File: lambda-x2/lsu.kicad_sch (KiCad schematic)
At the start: 56 parts, among them Q5 BSS169H6327, Q6 BSS169H6327, Q7 BSS169H6327, Q8 BSS169H6327, U12 MCP6002T-I/SN, U3 MCP6002T-I/SN, U9 GS8332-SR

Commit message: cosmetic
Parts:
- TP10: value (none) -> Ip; footprint (none) -> TestPoint:TestPoint_Pad_D1.0mm
- TP11: value (none) -> Rtrim; footprint (none) -> TestPoint:TestPoint_Pad_D1.0mm
- TP12: value (none) -> Vm; footprint (none) -> TestPoint:TestPoint_Pad_D1.0mm
- TP3: value (none) -> Un_Sense; footprint (none) -> TestPoint:TestPoint_Pad_D1.0mm
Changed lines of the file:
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@@
       (effects (font (size 1.27 1.27)) (justify left) hide)
     )
-    (property "Value" "" (id 1) (at 172.72 113.03 0)
-      (effects (font (size 1.27 1.27)) (justify left))
-    )
-    (property "Footprint" "" (id 2) (at 175.26 116.84 0)
+    (property "Value" "Un_Sense" (id 1) (at 172.72 113.03 0)
+      (effects (font (size 1.27 1.27)) (justify left))
+    )
+    (property "Footprint" "TestPoint:TestPoint_Pad_D1.0mm" (id 2) (at 175.26 116.84 0)
       (effects (font (size 1.27 1.27)) hide)
     )
@@
       (effects (font (size 1.27 1.27)) (justify left) hide)
     )
-    (property "Value" "" (id 1) (at 83.82 213.36 0)
-      (effects (font (size 1.27 1.27)) (justify left))
-    )
-    (property "Footprint" "" (id 2) (at 86.36 217.17 0)
+    (property "Value" "Ip" (id 1) (at 83.82 213.36 0)
+      (effects (font (size 1.27 1.27)) (justify left))
+    )
+    (property "Footprint" "TestPoint:TestPoint_Pad_D1.0mm" (id 2) (at 86.36 217.17 0)
       (effects (font (size 1.27 1.27)) hide)
     )
@@
       (effects (font (size 1.27 1.27)) (justify left) hide)
     )
-    (property "Value" "" (id 1) (at 83.82 223.52 0)
-      (effects (font (size 1.27 1.27)) (justify left))
-    )
-    (property "Footprint" "" (id 2) (at 86.36 227.33 0)
+    (property "Value" "Rtrim" (id 1) (at 83.82 223.52 0)
+      (effects (font (size 1.27 1.27)) (justify left))
+    )
+    (property "Footprint" "TestPoint:TestPoint_Pad_D1.0mm" (id 2) (at 86.36 227.33 0)
       (effects (font (size 1.27 1.27)) hide)
     )
@@
       (effects (font (size 1.27 1.27)) (justify left) hide)
     )
-    (property "Value" "" (id 1) (at 85.09 67.31 0)
-      (effects (font (size 1.27 1.27)) (justify left))
-    )
-    (property "Footprint" "" (id 2) (at 87.63 71.12 0)
-      (effects (font (size 1.27 1.27)) hide)
-    )
+    (property "Value" "Vm" (id 1) (at 85.09 67.31 0)
+      (effects (font (size 1.27 1.27)) (justify left))
+    )
+    (property "Footprint" "TestPoint:TestPoint_Pad_D1.0mm" (id 2) (at 87.63 71.12 0)
+      (effects (font (size 1.27 1.27)) hide)
+    )

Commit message: Progress
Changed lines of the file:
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@@
     (pin "2")
   )
-  (symbol (lib_id "power:GND") (at 222.25 264.16 0) (unit 1)
+  (symbol (lib_name "GND_6") (lib_id "power:GND") (at 222.25 264.16 0) (unit 1)
     (in_bom yes) (on_board yes)
     (property "Reference" "#PWR0104" (id 0) (at 222.25 270.51 0)
       (effects (font (size 1.27 1.27)) hide)
     )
-    (property "Value" "GND" (id 1) (at 222.377 268.5542 0))
+    (property "Value" "" (id 1) (at 222.377 268.5542 0)
+      (effects (font (size 1.27 1.27)) hide)
+    )
     (property "Footprint" "" (id 2) (at 222.25 264.16 0)
       (effects (font (size 1.27 1.27)) hide)
@@
       (effects (font (size 1.27 1.27)) hide)
     )
-    (property "Value" "GND" (id 1) (at 117.983 131.3942 0))
+    (property "Value" "" (id 1) (at 117.983 131.3942 0)
+      (effects (font (size 1.27 1.27)) hide)
+    )
     (property "Footprint" "" (id 2) (at 118.11 127 0)
       (effects (font (size 1.27 1.27)) hide)
@@
     (pin "2")
   )
-  (symbol (lib_id "power:GND") (at 162.56 264.16 0) (mirror y) (unit 1)
+  (symbol (lib_name "GND_5") (lib_id "power:GND") (at 162.56 264.16 0) (mirror y) (unit 1)
     (in_bom yes) (on_board yes)
     (property "Reference" "#PWR0125" (id 0) (at 162.56 270.51 0)
       (effects (font (size 1.27 1.27)) hide)
     )
-    (property "Value" "GND" (id 1) (at 162.433 268.5542 0))
+    (property "Value" "" (id 1) (at 162.433 268.5542 0)
+      (effects (font (size 1.27 1.27)) hide)
+    )
     (property "Footprint" "" (id 2) (at 162.56 264.16 0)
       (effects (font (size 1.27 1.27)) hide)
@@
       (effects (font (size 1.27 1.27)) hide)
     )
-    (property "Value" "GND" (id 1) (at 222.25 172.72 0))
+    (property "Value" "" (id 1) (at 222.25 172.72 0)
+      (effects (font (size 1.27 1.27)) hide)
+    )
     (property "Footprint" "" (id 2) (at 222.25 168.91 0)
       (effects (font (size 1.27 1.27)) hide)
@@
     (pin "2")
   )
-  (symbol (lib_id "power:GND") (at 87.63 81.28 0) (mirror y) (unit 1)
+  (symbol (lib_name "GND_2") (lib_id "power:GND") (at 87.63 81.28 0) (mirror y) (unit 1)
     (in_bom yes) (on_board yes)
     (property "Reference" "#PWR0126" (id 0) (at 87.63 87.63 0)
       (effects (font (size 1.27 1.27)) hide)
     )
-    (property "Value" "GND" (id 1) (at 87.503 85.6742 0))
+    (property "Value" "" (id 1) (at 87.503 85.6742 0)
+      (effects (font (size 1.27 1.27)) hide)
+    )
     (property "Footprint" "" (id 2) (at 87.63 81.28 0)
       (effects (font (size 1.27 1.27)) hide)
@@
     (pin "2")
   )
-  (symbol (lib_id "power:GND") (at 111.76 60.96 0) (mirror x) (unit 1)
+  (symbol (lib_name "GND_3") (lib_id "power:GND") (at 111.76 60.96 0) (mirror x) (unit 1)
     (in_bom yes) (on_board yes)
     (property "Reference" "#PWR0139" (id 0) (at 111.76 54.61 0)
       (effects (font (size 1.27 1.27)) hide)
     )
-    (property "Value" "GND" (id 1) (at 111.887 56.5658 0))
+    (property "Value" "" (id 1) (at 111.887 56.5658 0)
+      (effects (font (size 1.27 1.27)) hide)
+    )
     (property "Footprint" "" (id 2) (at 111.76 60.96 0)
       (effects (font (size 1.27 1.27)) hide)
@@
   (symbol (lib_id "Amplifier_Operational:MCP6002-xMS") (at 205.74 158.75 0) (mirror y) (unit 3)
     (in_bom yes) (on_board yes)
-    (property "Reference" "U12" (id 0) (at 201.93 152.4 0))
-    (property "Value" "MCP6002T-I/SN" (id 1) (at 201.295 154.94 0))
+    (property "Reference" "U12" (id 0) (at 201.93 157.48 0))
+    (property "Value" "MCP6002T-I/SN" (id 1) (at 198.12 160.02 0))
     (property "Footprint" "Package_SO:SOIC-8_3.9x4.9mm_P1.27mm" (id 2) (at 205.74 158.75 0)
       (effects (font (size 1.27 1.27)) hide)
@@
       (effects (font (size 1.27 1.27)) hide)
     )
-    (property "Value" "+3.3V" (id 1) (at 222.631 144.1958 0))
+    (property "Value" "" (id 1) (at 222.631 144.1958 0))
     (property "Footprint" "" (id 2) (at 222.25 148.59 0)
       (effects (font (size 1.27 1.27)) hide)
@@
       (effects (font (size 1.27 1.27)) hide)
     )
-    (property "Value" "VDDA" (id 1) (at 222.631 239.4458 0))
+    (property "Value" "" (id 1) (at 222.631 239.4458 0))
     (property "Footprint" "" (id 2) (at 222.25 243.84 0)
       (effects (font (size 1.27 1.27)) hide)
@@
     (pin "2")
   )
-  (symbol (lib_id "power:GND") (at 118.11 148.59 270) (mirror x) (unit 1)
+  (symbol (lib_name "GND_4") (lib_id "power:GND") (at 118.11 148.59 270) (mirror x) (unit 1)
     (in_bom yes) (on_board yes)
     (property "Reference" "#PWR0127" (id 0) (at 111.76 148.59 0)
       (effects (font (size 1.27 1.27)) hide)
     )
-    (property "Value" "GND" (id 1) (at 113.7158 148.463 0))
+    (property "Value" "" (id 1) (at 113.7158 148.463 0)
+      (effects (font (size 1.27 1.27)) hide)
+    )
     (property "Footprint" "" (id 2) (at 118.11 148.59 0)
       (effects (font (size 1.27 1.27)) hide)

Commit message: Progress
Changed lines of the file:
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@@
       (effects (font (size 1.27 1.27)) hide)
     )
-    (property "Value" "" (id 1) (at 222.377 268.5542 0)
+    (property "Value" "GND" (id 1) (at 222.377 268.5542 0)
       (effects (font (size 1.27 1.27)) hide)
     )
@@
       (effects (font (size 1.27 1.27)) hide)
     )
-    (property "Value" "" (id 1) (at 117.983 131.3942 0)
+    (property "Value" "GND" (id 1) (at 117.983 131.3942 0)
       (effects (font (size 1.27 1.27)) hide)
     )
@@
       (effects (font (size 1.27 1.27)) hide)
     )
-    (property "Value" "" (id 1) (at 162.433 268.5542 0)
+    (property "Value" "GND" (id 1) (at 162.433 268.5542 0)
       (effects (font (size 1.27 1.27)) hide)
     )
@@
       (effects (font (size 1.27 1.27)) hide)
     )
-    (property "Value" "" (id 1) (at 222.25 172.72 0)
+    (property "Value" "GND" (id 1) (at 222.25 172.72 0)
       (effects (font (size 1.27 1.27)) hide)
     )
@@
       (effects (font (size 1.27 1.27)) hide)
     )
-    (property "Value" "" (id 1) (at 87.503 85.6742 0)
+    (property "Value" "GND" (id 1) (at 87.503 85.6742 0)
       (effects (font (size 1.27 1.27)) hide)
     )
@@
       (effects (font (size 1.27 1.27)) hide)
     )
-    (property "Value" "" (id 1) (at 111.887 56.5658 0)
+    (property "Value" "GND" (id 1) (at 111.887 56.5658 0)
       (effects (font (size 1.27 1.27)) hide)
     )
@@
       (effects (font (size 1.27 1.27)) hide)
     )
-    (property "Value" "" (id 1) (at 222.631 144.1958 0))
+    (property "Value" "+3.3V" (id 1) (at 222.631 144.1958 0))
     (property "Footprint" "" (id 2) (at 222.25 148.59 0)
       (effects (font (size 1.27 1.27)) hide)
@@
       (effects (font (size 1.27 1.27)) hide)
     )
-    (property "Value" "" (id 1) (at 222.631 239.4458 0))
+    (property "Value" "VDDA" (id 1) (at 222.631 239.4458 0))
     (property "Footprint" "" (id 2) (at 222.25 243.84 0)
       (effects (font (size 1.27 1.27)) hide)
@@
       (effects (font (size 1.27 1.27)) hide)
     )
-    (property "Value" "" (id 1) (at 113.7158 148.463 0)
-      (effects (font (size 1.27 1.27)) hide)
-    )
+    (property "Value" "GND" (id 1) (at 113.7158 148.463 0)
+      (effects (font (size 1.27 1.27)) hide)
+    )

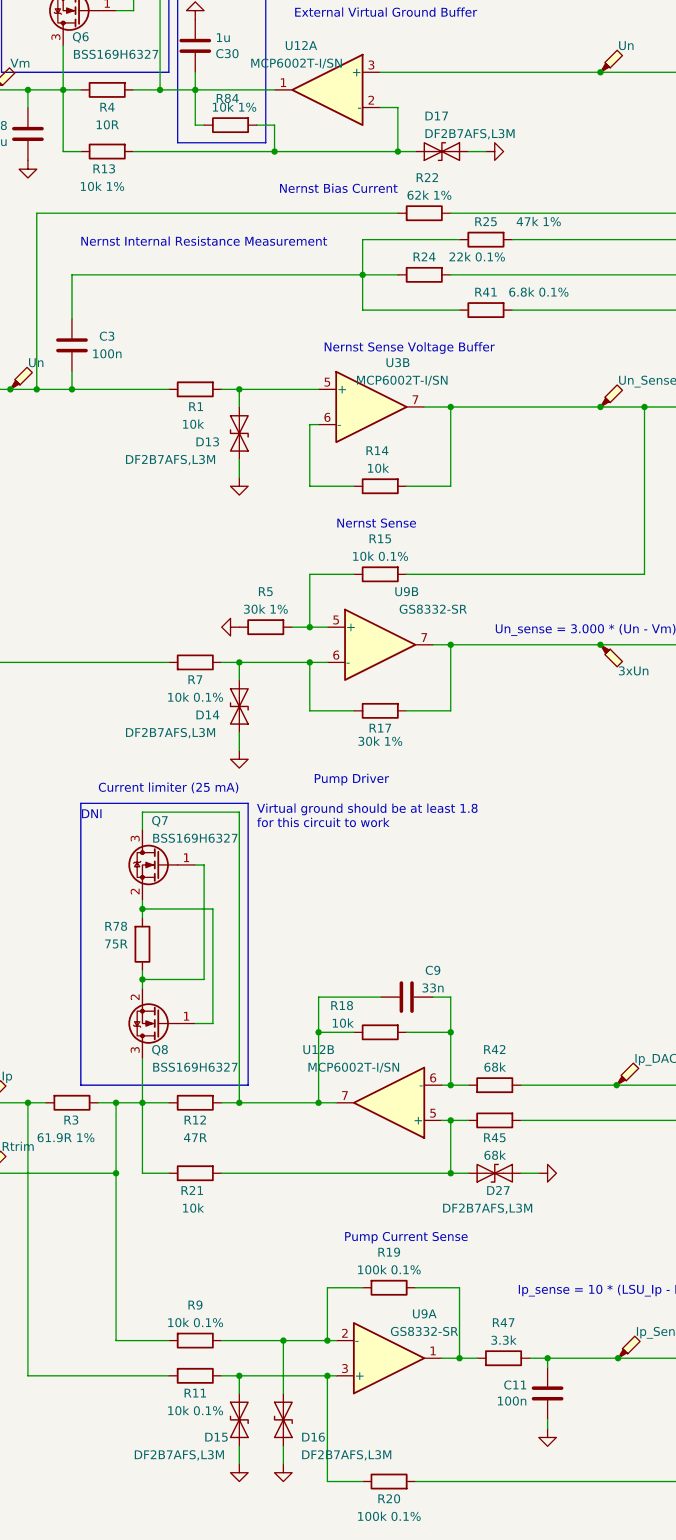
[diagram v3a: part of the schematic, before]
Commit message: Replace DF2B7AFS,L3M to ESD5V0D9B, fix mcp6002 LCSC
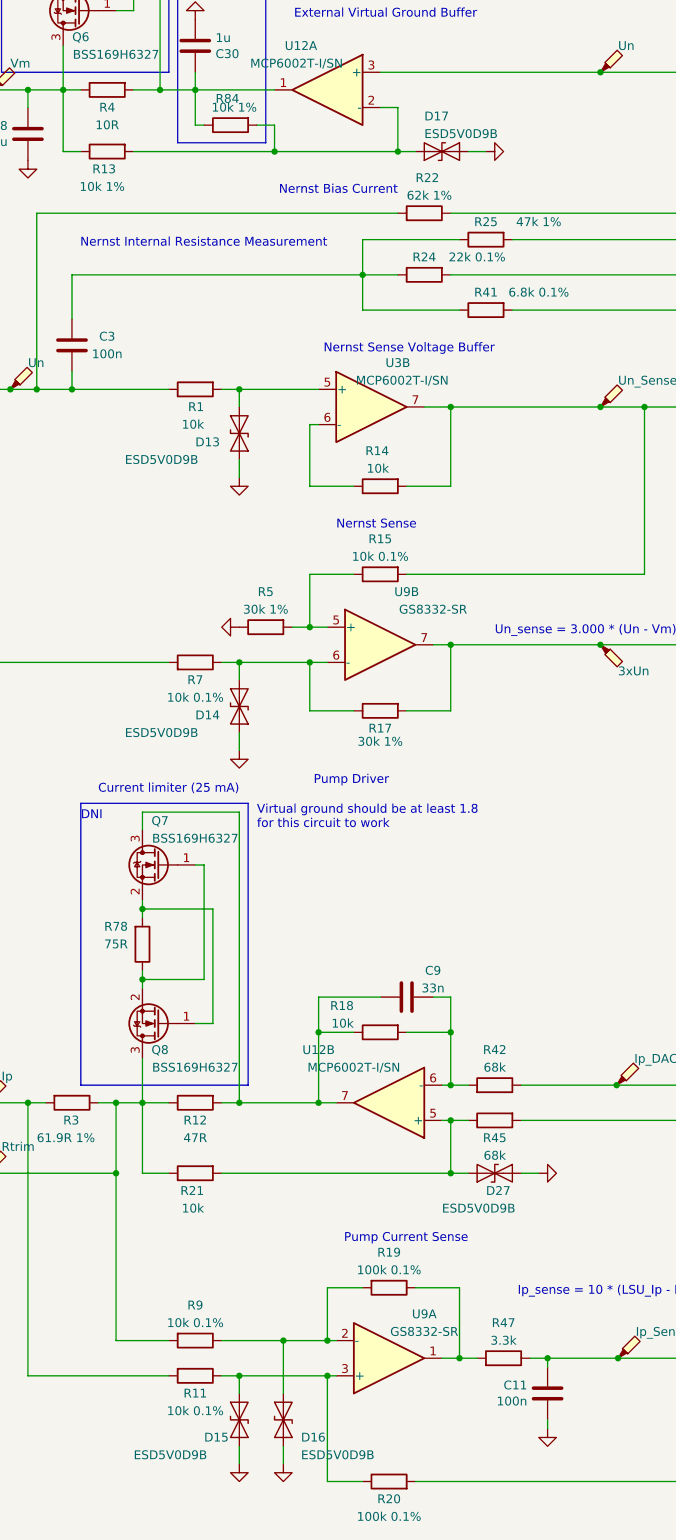
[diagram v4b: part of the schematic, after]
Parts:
- D13, D14, D15, D16, D17, D27: value DF2B7AFS,L3M -> ESD5V0D9B; LCSC C1972965 -> C484329
- U12, U3: LCSC C50282 -> C7377
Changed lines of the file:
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@@
       (effects (font (size 1.27 1.27)) (justify left))
     )
-    (property "Value" "DF2B7AFS,L3M" (id 1) (at 144.78 77.47 0)
+    (property "Value" "ESD5V0D9B" (id 1) (at 144.78 77.47 0)
       (effects (font (size 1.27 1.27)) (justify left))
     )
@@
       (effects (font (size 1.27 1.27)) hide)
     )
-    (property "LCSC" "C1972965" (id 4) (at 147.32 80.01 90)
+    (property "LCSC" "C484329" (id 4) (at 147.32 80.01 90)
       (effects (font (size 1.27 1.27)) hide)
     )
@@
       (effects (font (size 1.27 1.27)) hide)
     )
-    (property "LCSC" "C50282" (id 4) (at 205.74 68.58 0)
+    (property "LCSC" "C7377" (id 4) (at 205.74 68.58 0)
       (effects (font (size 1.27 1.27)) hide)
     )
@@
       (effects (font (size 1.27 1.27)) (justify left))
     )
-    (property "Value" "DF2B7AFS,L3M" (id 1) (at 127 267.97 90)
+    (property "Value" "ESD5V0D9B" (id 1) (at 127 267.97 90)
       (effects (font (size 1.27 1.27)) (justify left))
     )
@@
       (effects (font (size 1.27 1.27)) hide)
     )
-    (property "LCSC" "C1972965" (id 4) (at 124.46 262.89 90)
+    (property "LCSC" "C484329" (id 4) (at 124.46 262.89 90)
       (effects (font (size 1.27 1.27)) hide)
     )
@@
       (effects (font (size 1.27 1.27)) (justify left))
     )
-    (property "Value" "DF2B7AFS,L3M" (id 1) (at 101.6 163.83 90)
+    (property "Value" "ESD5V0D9B" (id 1) (at 101.6 163.83 90)
       (effects (font (size 1.27 1.27)) (justify left))
     )
@@
       (effects (font (size 1.27 1.27)) hide)
     )
-    (property "LCSC" "C1972965" (id 4) (at 118.11 160.02 90)
+    (property "LCSC" "C484329" (id 4) (at 118.11 160.02 90)
       (effects (font (size 1.27 1.27)) hide)
     )
@@
       (effects (font (size 1.27 1.27)) (justify left))
     )
-    (property "Value" "DF2B7AFS,L3M" (id 1) (at 102.87 267.97 90)
+    (property "Value" "ESD5V0D9B" (id 1) (at 102.87 267.97 90)
       (effects (font (size 1.27 1.27)) (justify left))
     )
@@
       (effects (font (size 1.27 1.27)) hide)
     )
-    (property "LCSC" "C1972965" (id 4) (at 118.11 262.89 90)
+    (property "LCSC" "C484329" (id 4) (at 118.11 262.89 90)
       (effects (font (size 1.27 1.27)) hide)
     )
@@
       (effects (font (size 1.27 1.27)) hide)
     )
-    (property "LCSC" "C50282" (id 4) (at 130.81 71.12 0)
+    (property "LCSC" "C7377" (id 4) (at 130.81 71.12 0)
       (effects (font (size 1.27 1.27)) hide)
     )
@@
       (effects (font (size 1.27 1.27)) (justify left))
     )
-    (property "Value" "DF2B7AFS,L3M" (id 1) (at 147.32 232.41 0)
+    (property "Value" "ESD5V0D9B" (id 1) (at 147.32 232.41 0)
       (effects (font (size 1.27 1.27)) (justify left))
     )
@@
       (effects (font (size 1.27 1.27)) hide)
     )
-    (property "LCSC" "C1972965" (id 4) (at 154.94 227.33 90)
+    (property "LCSC" "C484329" (id 4) (at 154.94 227.33 90)
       (effects (font (size 1.27 1.27)) hide)
     )
@@
       (effects (font (size 1.27 1.27)) hide)
     )
-    (property "LCSC" "C50282" (id 4) (at 205.74 158.75 0)
+    (property "LCSC" "C7377" (id 4) (at 205.74 158.75 0)
       (effects (font (size 1.27 1.27)) hide)
     )
@@
       (effects (font (size 1.27 1.27)) hide)
     )
-    (property "LCSC" "C50282" (id 4) (at 224.79 158.75 0)
+    (property "LCSC" "C7377" (id 4) (at 224.79 158.75 0)
       (effects (font (size 1.27 1.27)) hide)
     )
@@
       (effects (font (size 1.27 1.27)) hide)
     )
-    (property "LCSC" "C50282" (id 4) (at 139.7 217.17 0)
+    (property "LCSC" "C7377" (id 4) (at 139.7 217.17 0)
       (effects (font (size 1.27 1.27)) hide)
     )
@@
       (effects (font (size 1.27 1.27)) hide)
     )
-    (property "LCSC" "C50282" (id 4) (at 137.16 116.84 0)
+    (property "LCSC" "C7377" (id 4) (at 137.16 116.84 0)
       (effects (font (size 1.27 1.27)) hide)
     )
@@
       (effects (font (size 1.27 1.27)) (justify left))
     )
-    (property "Value" "DF2B7AFS,L3M" (id 1) (at 101.6 124.46 90)
+    (property "Value" "ESD5V0D9B" (id 1) (at 101.6 124.46 90)
       (effects (font (size 1.27 1.27)) (justify left))
     )
@@
       (effects (font (size 1.27 1.27)) hide)
     )
-    (property "LCSC" "C1972965" (id 4) (at 118.11 120.65 90)
-      (effects (font (size 1.27 1.27)) hide)
-    )
+    (property "LCSC" "C484329" (id 4) (at 118.11 120.65 90)
+      (effects (font (size 1.27 1.27)) hide)
+    )
